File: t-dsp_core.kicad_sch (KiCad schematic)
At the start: 157 parts, among them IC1 Logic Level Shifter - 74HCT2G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, J1 HDR_A_OUTER Teensy-domain, J2 HDR_A_INNER Teensy-domain, J3 HDR_B_OUTER S3-domain, J4 HDR_B_INNER S3-domain, T108 Tab, T109 Tab, T110 Tab, T111 Tab, U1 Teensy 4.1 - DEVKIT, U11 Dual Buffer - SN74LVC2G125DCTR, U13 ESP32-S3-WROOM-1-N16R2, U15 LT3045EMSE#TRPBF, U16 THVD1450DR, U17 ISO7762DW, U18 TEA1-0505HI, U19 SRC4382IPFBR, U20 TLV75718PDRVR, U21 74LVC157APW, U22 IDC777-1, U23 74LVC157APW, U24 AP63203WU, U3 Power Mux & Protect - TPS2116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, U4 Optoisolators - H11L1SM - 6-S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, U5 Dual Buffer - SN74LVC2G125DCTR, U6 Dual Buffer - SN74LVC2G125DCTR, U7 Dual Buffer - SN74LVC2G125DCTR, U8 Dual Buffer - SN74LVC2G125DCTR, U9 Dual Buffer - 74HCT2G17GW,125, Y1 24.576MHz

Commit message: Spin 2 stage 8: DNP/excluded audit and stale notes
- C10/C11 (dnp, excluded) and H1-H4 (excluded) removed
- R19/R53/C4/C5 were excluded-from-board: re-placed on-board at the same
  coordinates with footprints and LCSC numbers; netlist unchanged
- 35 obsolete text notes removed; orphaned GND symbols and hole NC flags removed
- change map section 17

Co-Authored-By: Claude Fable 5.1 <noreply@anthropic.com>
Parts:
- removed C10, C11: 0.1uF, project_fp:C_0805_2012Metric_Pad1.15x1.40mm_HandSolder, symbol TEENSY_4.0_ESP32_AUDIO-rescue:C_Small-Device
- removed C4, C5: 0.1 uF, project_fp:C_0805_2012Metric_Pad1.15x1.40mm_HandSolder, symbol TEENSY_4.0_ESP32_AUDIO-rescue:C_Small-Device
- removed H1, H2, H3, H4: MountingHole_Pad, MountingHole:MountingHole_3.2mm_M3_DIN965_Pad, symbol Mechanical:MountingHole_Pad
- added C4, C5: 0.1 uF, project_fp:C_0805_2012Metric_Pad1.15x1.40mm_HandSolder, symbol Device:C
- R19, R53: LCSC TYPE SMD -> (none); LCSC_MPN 0805W8F1002T5E -> (none); LCSC_Manufacturer UNI-ROYAL -> (none); Package / Case R0805 -> (none)
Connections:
- net ESP32_EN: now also C4.1
- net ESP32_IO0: now also C5.1
- net GND: now also C4.2, C5.2
- no-connect marks 74 -> 70
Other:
- note removed: "3 PIN MIDI"
- note removed: "3.3v DIGITAL RAIL"
- note removed: "5V PRIORITY SWITCHOVER + INRUSH LIMITING"
- note removed: "AUDIO MODULE"
- note removed: "Changed to SPH0645LM4H-B for Target use: Voice/audio capture (speech, speakerphone, voice assistants, etc.)"
- note removed: "ESP32"
- note removed: "ESP32 S3"
- note removed: "ETHERNET"
- note removed: "HAT MOUNTING POINTS"
- note removed: "I2S BUFFER + EXPANSION PORTS"
- note removed: "KiCad 8-Layer Stackup: F.Cu - TOP: Components, ANALOG routes to jacks, ground fill In1.Cu - GND: Solid ground plane In2.Cu - SIG1: TDM/high-speed digital, ground fill In3.Cu - GND: Solid ground plane (isolation!) In4.Cu - SIG2: More TDM/digital signals, ground fill In5.Cu - PWR: Power planes (3.3V/5V) In6.Cu - GND: Solid ground plane B.Cu - BOTTOM: Components, ANALOG routes to jacks, ground fill"
- note removed: "MECHANICAL"
- note removed: "MIDI HEADER"
- note removed: "MUST VERIFY LINES AND PADS"
- note removed: "OPTICAL / TOSLINK IO"
- note removed: "PJRAS2X1S01X INSERT A (RED) RIGHT iNSERT B (WHITE) LEFT"
- note removed: "PLEASE CONFIRM LEFT/RIGHT PINS"
- note removed: "POWER SUPPLY"
- note removed: "RGB LED + HEADER"
- note removed: "SWITCHES"
- note removed: "T-DSP Desktop Soundcard"
- note removed: "TEENSY 4"
- note removed: "TL1105WF160Q = 3.15mm actuator = hidden behind side panel by 1.1mm TL1105XF160Q = 5.85mm actuator = petruding from side panel by 1.35mm ACTUAL DISTANCE FROM EDGE = 4.25mm."
- note removed: "USB A HOST PORT"
- note removed: "USB B Option"
- note removed: "USB C DEVICE PORT"
- note removed: "USB C Option"
- note removed: "USB IN HEADER"
- note removed: "USB POWER FILTER"
- note removed: "https://idyl.io/how-to-add-usb-type-c-micro-usb-replacement/?amp"
- note removed: "https://www.pcbway.com/blog/PCB_Design_Tutorial/How_to_make_your_own_ESP32_breakout_board_with_minimal_circuit.html"
- note removed: "w a0 0a 41 # Configure GPIO1 as PDMCLK with drive active high and low w a0 0d 02 # Configure GPI1 as input"

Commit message: Spin 2 stage 9: function-scoped headers J1-J11 replace the four 2x22 edge blocks; S3 N16R8 (octal PSRAM) frees IO35-37, BT UART RX moves to IO3
Co-Authored-By: Claude Fable 5.1 <noreply@anthropic.com>
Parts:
- removed J1: HDR_A_OUTER Teensy-domain, Connector_PinHeader_2.54mm:PinHeader_2x22_P2.54mm_Vertical, symbol Connector_Generic:Conn_02x22_Odd_Even
- removed J2: HDR_A_INNER Teensy-domain, Connector_PinHeader_2.54mm:PinHeader_2x22_P2.54mm_Vertical, symbol Connector_Generic:Conn_02x22_Odd_Even
- removed J3: HDR_B_OUTER S3-domain, Connector_PinHeader_2.54mm:PinHeader_2x22_P2.54mm_Vertical, symbol Connector_Generic:Conn_02x22_Odd_Even
- removed J4: HDR_B_INNER S3-domain, Connector_PinHeader_2.54mm:PinHeader_2x22_P2.54mm_Vertical, symbol Connector_Generic:Conn_02x22_Odd_Even
- added J1: J_PWR, Connector_PinHeader_2.54mm:PinHeader_2x06_P2.54mm_Vertical, symbol Connector_Generic:Conn_02x06_Odd_Even
- added J10: J_DMX, Connector_PinHeader_2.54mm:PinHeader_1x05_P2.54mm_Vertical, symbol Connector_Generic:Conn_01x05
- added J11: J_LED, Connector_PinHeader_2.54mm:PinHeader_1x05_P2.54mm_Vertical, symbol Connector_Generic:Conn_01x05
- added J2: J_TDM, Connector_PinHeader_2.54mm:PinHeader_2x13_P2.54mm_Vertical, symbol Connector_Generic:Conn_02x13_Odd_Even
- added J3: J_T, Connector_PinHeader_2.54mm:PinHeader_2x12_P2.54mm_Vertical, symbol Connector_Generic:Conn_02x12_Odd_Even
- added J4: J_USBH, Connector_PinHeader_2.54mm:PinHeader_1x05_P2.54mm_Vertical, symbol Connector_Generic:Conn_01x05
- added J5: J_MIDI, Connector_PinHeader_2.54mm:PinHeader_2x04_P2.54mm_Vertical, symbol Connector_Generic:Conn_02x04_Odd_Even
- added J6: J_SPDIF, Connector_PinHeader_2.54mm:PinHeader_2x11_P2.54mm_Vertical, symbol Connector_Generic:Conn_02x11_Odd_Even
- added J7: J_AUX, Connector_PinHeader_2.54mm:PinHeader_2x05_P2.54mm_Vertical, symbol Connector_Generic:Conn_02x05_Odd_Even
- added J8: J_S3, Connector_PinHeader_2.54mm:PinHeader_2x15_P2.54mm_Vertical, symbol Connector_Generic:Conn_02x15_Odd_Even
- added J9: J_USB3, Connector_PinHeader_2.54mm:PinHeader_1x05_P2.54mm_Vertical, symbol Connector_Generic:Conn_01x05
- U13: value ESP32-S3-WROOM-1-N16R2 -> ESP32-S3-WROOM-1-N16R8; LCSC C2913205 -> C2913202; LCSC_MPN ESP32-S3-WROOM-1-N16R2 -> ESP32-S3-WROOM-1-N16R8
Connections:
- net S3_IO3 is gone; now on net BT_UART_RX: U13.15 (IO3)
- net 14_SPDIF_OUT: now also J3.3 (Pin_3)
- net 15_SPDIF_IN: now also J3.4 (Pin_4)
- net 3.3V: now also J1.9 (Pin_9)
- net 3.3V_DIG: now also J1.10 (Pin_10)
- net 32_OUT1B: now also J3.20 (Pin_20)
- net 34_RX8_RESET2: now also J3.10 (Pin_10)
- net 35_TX8_RESET: now also J3.9 (Pin_9)
- net 53_T_PROG: now also J3.11 (Pin_11)
- net 54_ON_OFF: now also J3.12 (Pin_12)
- net 5V: now also J1.5 (Pin_5), J1.6 (Pin_6), J11.5 (Pin_5), J9.5 (Pin_5)
- net 5V_IN: now also J1.1 (Pin_1), J1.2 (Pin_2)
- net 5V_ISO: now also J10.5 (Pin_5)
- net 6_OUT1D+: now also J2.16 (Pin_16)
- net 7_OUT1A+: now also J2.15 (Pin_15)
- net 8_IN1: now also J2.17 (Pin_17)
- net 9_OUT1C_INPUT: now also J2.18 (Pin_18)
- net AUX_I2S_BCK: now also J7.3 (Pin_3)
- net AUX_I2S_DIN: now also J7.7 (Pin_7)
- net AUX_I2S_LRCK: now also J7.6 (Pin_6)
- net AUX_I2S_OUT: now also J7.8 (Pin_8)
- net BCLK1+TDM1: now also J2.7 (Pin_7)
- net BCLK1+TDM2: now also J2.8 (Pin_8)
- net BT_UART_RX: no longer U13.28 (IO35)
- net CRX3: now also J3.7 (Pin_7)
- net CS: now also J8.14 (Pin_14)
- net DC: now also J8.17 (Pin_17)
- net DMX_A: now also J10.2 (Pin_2)
- net DMX_B: now also J10.3 (Pin_3)
- net DMX_GND: now also J10.1 (Pin_1), J10.4 (Pin_4)
- net ESP32_EN: now also J8.5 (Pin_5)
- net ESP32_IO0: now also J8.6 (Pin_6)
- net ESP32_IO1: now also J8.3 (Pin_3)
- net ESP32_IO21_SDA: now also J8.9 (Pin_9)
- net ESP32_IO22_SCL: now also J8.10 (Pin_10)
- net ESP32_IO3: now also J8.4 (Pin_4)
- net ESP32_LED_OUT: now also J11.4 (Pin_4)
- net GND: now also J1.12 (Pin_12), J1.3 (Pin_3), J1.4 (Pin_4), J1.7 (Pin_7), J1.8 (Pin_8), J11.1 (Pin_1), J11.3 (Pin_3), J2.1 (Pin_1), J2.10 (Pin_10), J2.13 (Pin_13), J2.14 (Pin_14), J2.19 (Pin_19), J2.2 (Pin_2), J2.20 (Pin_20), J2.25 (Pin_25), J2.26 (Pin_26), J2.5 (Pin_5), J2.6 (Pin_6), J2.9 (Pin_9), J3.1 (Pin_1), J3.15 (Pin_15), J3.16 (Pin_16), J3.2 (Pin_2), J3.21 (Pin_21), J3.23 (Pin_23), J3.24 (Pin_24), J3.5 (Pin_5), J3.6 (Pin_6), J4.1 (Pin_1), J4.4 (Pin_4), J5.7 (Pin_7), J5.8 (Pin_8), J6.1 (Pin_1), J6.10 (Pin_10), J6.13 (Pin_13), J6.14 (Pin_14), J6.17 (Pin_17), J6.18 (Pin_18), J6.2 (Pin_2), J6.21 (Pin_21), J6.22 (Pin_22), J6.5 (Pin_5), J6.6 (Pin_6), J6.9 (Pin_9), J7.1 (Pin_1), J7.10 (Pin_10), J7.2 (Pin_2), J7.4 (Pin_4), J7.5 (Pin_5), J7.9 (Pin_9), J8.1 (Pin_1), J8.15 (Pin_15), J8.16 (Pin_16), J8.2 (Pin_2), J8.23 (Pin_23), J8.24 (Pin_24), J8.28 (Pin_28), J8.29 (Pin_29), J8.30 (Pin_30), J8.7 (Pin_7), J8.8 (Pin_8), J9.1 (Pin_1), J9.4 (Pin_4)
- net GPIO34: now also J8.25 (Pin_25)
- net GPIO35: now also J8.26 (Pin_26)
- net HOST_5V: now also J4.5 (Pin_5)
- net HOST_D1+: now also J4.3 (Pin_3)
- net HOST_D1-: now also J4.2 (Pin_2)
- net LRCK1+TDM1: now also J2.11 (Pin_11)
- net LRCK1+TDM2: now also J2.12 (Pin_12)
- net MCLK1+TDM1: now also J2.3 (Pin_3)
- net MCLK1+TDM2: now also J2.4 (Pin_4)
- net MCLK2: now also J3.22 (Pin_22)
- net MIDI_IN_4: now also J5.1 (Pin_1)
- net MIDI_IN_5: now also J5.2 (Pin_2)
- net MIDI_OUT_4: now also J5.3 (Pin_3)
- net MIDI_OUT_5: now also J5.4 (Pin_4)
- net MIDI_THRU_4: now also J5.5 (Pin_5)
- net MIDI_THRU_5: now also J5.6 (Pin_6)
- net OUTPUTA: now also J8.20 (Pin_20)
- net OUTPUTB: now also J8.21 (Pin_21)
- net RESET: now also J8.18 (Pin_18)
- net S3_IO45: now also J8.27 (Pin_27)
- net S3_USB_DN: now also J9.2 (Pin_2)
- net S3_USB_DP: now also J9.3 (Pin_3)
- net SCK: now also J8.11 (Pin_11)
- net SCL0: now also J2.23 (Pin_23)
- net SCL1: now also J2.24 (Pin_24)
- net SDA0: now also J2.21 (Pin_21)
- net SDA1: now also J2.22 (Pin_22)
- net SDI: now also J8.12 (Pin_12)
- net SDO: now also J8.13 (Pin_13)
- net SPDIF_RX1N: now also J6.4 (Pin_4)
- net SPDIF_RX1P: now also J6.3 (Pin_3)
- net SPDIF_RX2N: now also J6.8 (Pin_8)
- net SPDIF_RX2P: now also J6.7 (Pin_7)
- net SPDIF_RX3N: now also J6.12 (Pin_12)
- net SPDIF_RX3P: now also J6.11 (Pin_11)
- net SPDIF_RX4N: now also J6.16 (Pin_16)
- net SPDIF_RX4P: now also J6.15 (Pin_15)
- net SPDIF_TXN: now also J6.20 (Pin_20)
- net SPDIF_TXP: now also J6.19 (Pin_19)
- net SWITCH: now also J8.22 (Pin_22)
- net TEENSY_LED_OUT: now also J11.2 (Pin_2)
- net TRX3: now also J3.8 (Pin_8)
- net T_22: now also J3.17 (Pin_17)
- net T_26: now also J3.18 (Pin_18)
- net T_27: now also J3.19 (Pin_19)
- net T_BUTTON1: now also J3.13 (Pin_13)
- net T_BUTTON2: now also J3.14 (Pin_14)
- net T_CS: now also J8.19 (Pin_19)
- net V_BAT: now also J1.11 (Pin_11)
- net S3_IO36: no longer names the net of U13.29 (IO36)
- net S3_IO37: no longer names the net of U13.30 (IO37)
- no-connect marks 70 -> 60

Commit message: Spin 2 stage 9b: J12 J_ETH header, PSRAM and Ethernet notes on the sheet, change map sections 3/10/11/13/14/15 rewritten for the function-scoped headers
Co-Authored-By: Claude Fable 5.1 <noreply@anthropic.com>
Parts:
- added J12: J_ETH, Connector_PinHeader_2.54mm:PinHeader_2x04_P2.54mm_Vertical, symbol Connector_Generic:Conn_02x04_Odd_Even
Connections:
- net GND: now also J12.3 (Pin_3), J12.4 (Pin_4), J12.8 (Pin_8)
- new net ETH_LED: J12.7 (Pin_7)
- new net ETH_R+: J12.1 (Pin_1)
- new net ETH_R-: J12.2 (Pin_2)
- new net ETH_T+: J12.5 (Pin_5)
- new net ETH_T-: J12.6 (Pin_6)
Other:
- note added: "J_ETH: Teensy 4.1 Ethernet pads 60-65 (R+ R- T+ T- LED GND, 2 mm 2x3 on the Teensy bottom).\nPENDING: change U1 to project_sch:Teensy4.1 in eeschema, label pins 60=ETH_R+ 61=ETH_LED 62=ETH_T- 63=ETH_T+ 64=GND 65=ETH_R-,\nand restore pads 60-65 in Teensy41_mod3 (they exist in Teensy41.kicad_mod). Magnetics + RJ45 live on the backplane."
- note added: "U1 Teensy 4.1 memory: fit 2x APS6404L-3SQR-SN (8 MB PSRAM each, 16 MB total, EXTMEM) on the Teensy's own bottom-side SOIC-8 pads\nfor loop recording, echo and reverb buffers. Optional W25Q128 QSPI flash on the second pad if 8 MB PSRAM + flash is preferred.\nPCB rule: no parts or pads on the core top side under the Teensy footprint (SOIC-8 bodies 1.2 mm tall); Teensy sits on 2.54 mm headers."
- note added: "U13 = ESP32-S3-WROOM-1-N16R8 (16 MB flash + 8 MB OCTAL PSRAM, needed for Spotify/cspot stream buffering).\nOctal PSRAM owns IO35/IO36/IO37 -> those module pins are NC. BT UART RX therefore uses IO3 (not IO35).\nDo not substitute an R2 (quad) module without re-checking: R2 frees IO35-37 but 2 MB PSRAM is too small for Spotify."

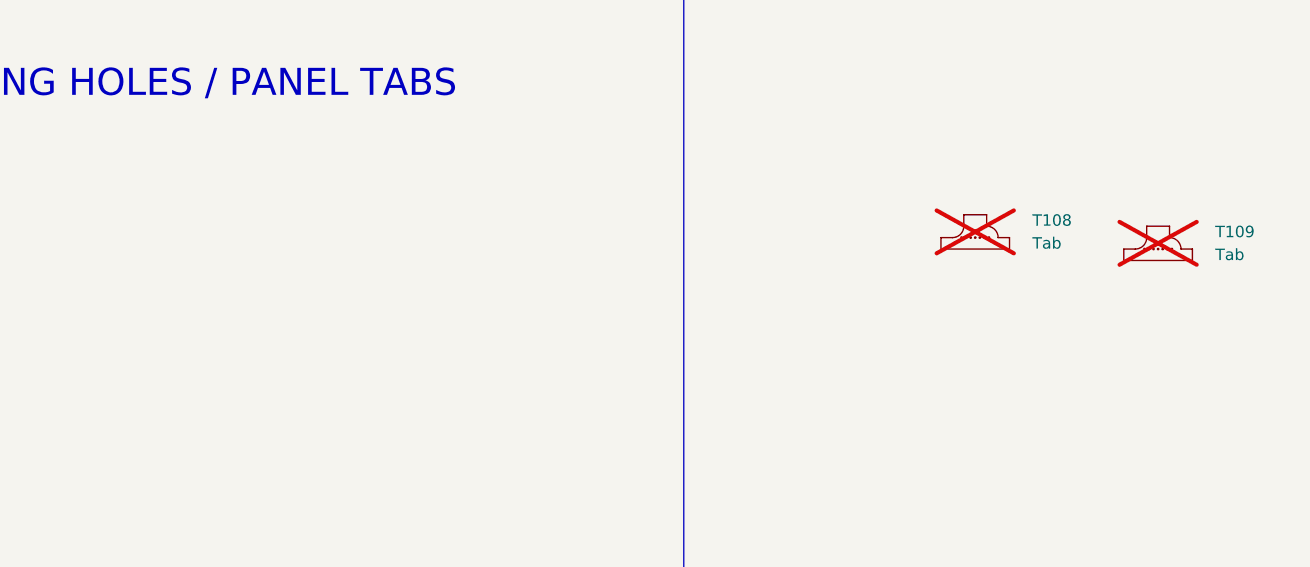
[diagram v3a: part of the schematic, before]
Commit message: Spin 2 stage 10b: H1-H4 M3 mounting holes in the schematic (KiCad discarded the PCB-only holes); change map note
Co-Authored-By: Claude Fable 5.1 <noreply@anthropic.com>
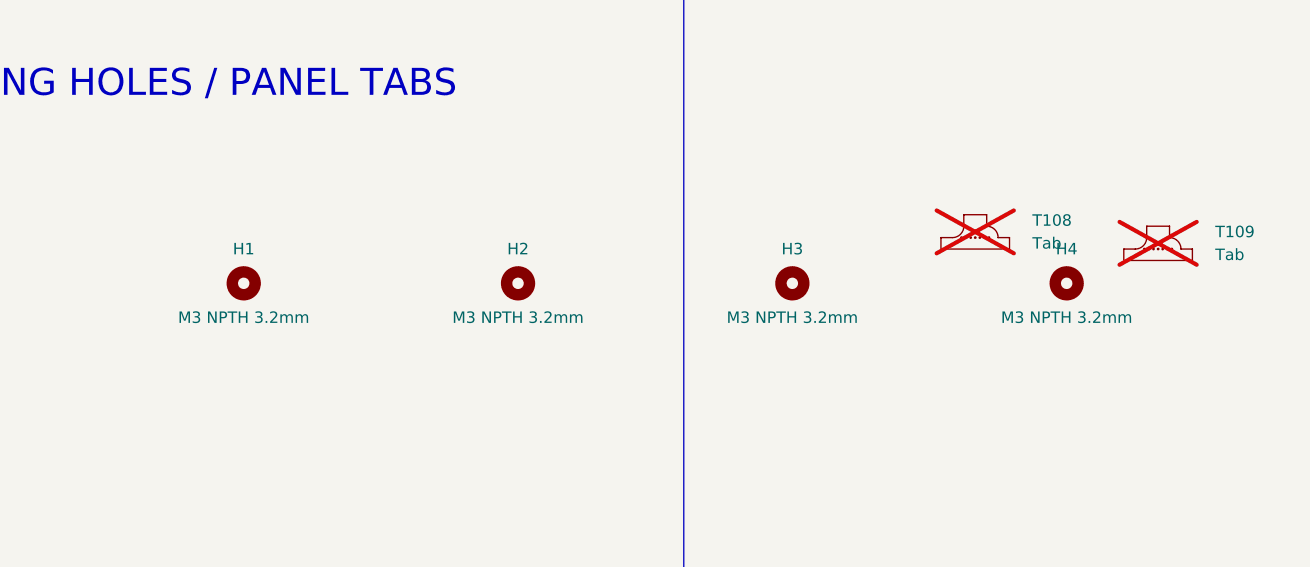
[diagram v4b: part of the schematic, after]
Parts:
- added H1, H2, H3, H4: M3 NPTH 3.2mm, MountingHole:MountingHole_3.2mm_M3, symbol Mechanical:MountingHole
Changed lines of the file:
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@@
         (size 3 3)))
 )
+  (text "J_ETH: Teensy 4.1 Ethernet pads 60-65 (R+ R- T+ T- LED GND, 2 mm 2x3 on the Teensy bottom).\\nPENDING: change U1 to project_sch:Teensy4.1 in eeschema, label pins 60=ETH_R+ 61=ETH_LED 62=ETH_T- 63=ETH_T+ 64=GND 65=ETH_R-,\\nand restore pads 60-65 in Teensy41_mod3 (they exist in Teensy41.kicad_mod). Magnetics + RJ45 live on the backplane."
+    (at 560.07 300.99 0)
+    (effects
+      (font
+        (size 1.27 1.27)))
+)
+  (text "U13 = ESP32-S3-WROOM-1-N16R8 (16 MB flash + 8 MB OCTAL PSRAM, needed for Spotify/cspot stream buffering).\\nOctal PSRAM owns IO35/IO36/IO37 -> those module pins are NC. BT UART RX therefore uses IO3 (not IO35).\\nDo not substitute an R2 (quad) module without re-checking: R2 frees IO35-37 but 2 MB PSRAM is too small for Spotify."
+    (at -320.04 570.23 0)
+    (effects
+      (font
+        (size 1.27 1.27)))
+)
+  (text "U1 Teensy 4.1 memory: fit 2x APS6404L-3SQR-SN (8 MB PSRAM each, 16 MB total, EXTMEM) on the Teensy's own bottom-side SOIC-8 pads\\nfor loop recording, echo and reverb buffers. Optional W25Q128 QSPI flash on the second pad if 8 MB PSRAM + flash is preferred.\\nPCB rule: no parts or pads on the core top side under the Teensy footprint (SOIC-8 bodies 1.2 mm tall); Teensy sits on 2.54 mm headers."
+    (at 95.25 338.14 0)
+    (effects
+      (font
+        (size 1.27 1.27)))
+)
   (label "DMX_RO_ISO"
     (at -224.79 924.56 0)
@@
           (reference "J12")
           (unit 1)))))
+  (symbol
+    (lib_id "Mechanical:MountingHole")
+    (at 1029.97 640.08 0)
+    (unit 1)
+    (in_bom yes)
+    (on_board yes)
+    (dnp no)
+    (property "Reference" "H1"
+      (at 1029.97 636.27 0)
+      (effects
+        (font
+          (size 1.27 1.27))))
+    (property "Value" "M3 NPTH 3.2mm"
+      (at 1029.97 643.89 0)
+      (effects
+        (font
+          (size 1.27 1.27))))
+    (property "Footprint" "MountingHole:MountingHole_3.2mm_M3"
+      (at 1029.97 640.08 0)
+      (effects
+        (font
+          (size 1.27 1.27))
+        (hide yes)))
+    (property "Datasheet" ""
+      (at 1029.97 640.08 0)
+      (effects
+        (font
+          (size 1.27 1.27))
+        (hide yes)))
+    (instances
+      (project "t-dsp_core"
+        (path "/6a0ff39d-771d-410f-9e7c-006586d81d16"
+          (reference "H1")
+          (unit 1)))))
+  (symbol
+    (lib_id "Mechanical:MountingHole")
+    (at 1060.45 640.08 0)
+    (unit 1)
+    (in_bom yes)
+    (on_board yes)
+    (dnp no)
+    (property "Reference" "H2"
+      (at 1060.45 636.27 0)
+      (effects
+        (font
+          (size 1.27 1.27))))
+    (property "Value" "M3 NPTH 3.2mm"
+      (at 1060.45 643.89 0)
+      (effects
+        (font
+          (size 1.27 1.27))))
+    (property "Footprint" "MountingHole:MountingHole_3.2mm_M3"
+      (at 1060.45 640.08 0)
+      (effects
+        (font
+          (size 1.27 1.27))
+        (hide yes)))
+    (property "Datasheet" ""
+      (at 1060.45 640.08 0)
+      (effects
+        (font
+          (size 1.27 1.27))
+        (hide yes)))
+    (instances
+      (project "t-dsp_core"
+        (path "/6a0ff39d-771d-410f-9e7c-006586d81d16"
+          (reference "H2")
+          (unit 1)))))
+  (symbol
+    (lib_id "Mechanical:MountingHole")
+    (at 1090.93 640.08 0)
+    (unit 1)
+    (in_bom yes)
+    (on_board yes)
+    (dnp no)
+    (property "Reference" "H3"
+      (at 1090.93 636.27 0)
+      (effects
+        (font
+          (size 1.27 1.27))))
+    (property "Value" "M3 NPTH 3.2mm"
+      (at 1090.93 643.89 0)
+      (effects
+        (font
+          (size 1.27 1.27))))
+    (property "Footprint" "MountingHole:MountingHole_3.2mm_M3"
+      (at 1090.93 640.08 0)
+      (effects
+        (font
+          (size 1.27 1.27))
+        (hide yes)))
+    (property "Datasheet" ""
+      (at 1090.93 640.08 0)
+      (effects
+        (font
+          (size 1.27 1.27))
+        (hide yes)))
+    (instances
+      (project "t-dsp_core"
+        (path "/6a0ff39d-771d-410f-9e7c-006586d81d16"
+          (reference "H3")
+          (unit 1)))))
+  (symbol
+    (lib_id "Mechanical:MountingHole")
+    (at 1121.41 640.08 0)
+    (unit 1)
+    (in_bom yes)
+    (on_board yes)
+    (dnp no)
+    (property "Reference" "H4"
+      (at 1121.41 636.27 0)
+      (effects
+        (font
+          (size 1.27 1.27))))
+    (property "Value" "M3 NPTH 3.2mm"
+      (at 1121.41 643.89 0)
+      (effects
+        (font
+          (size 1.27 1.27))))
+    (property "Footprint" "MountingHole:MountingHole_3.2mm_M3"
+      (at 1121.41 640.08 0)
+      (effects
+        (font
+          (size 1.27 1.27))
+        (hide yes)))
+    (property "Datasheet" ""
+      (at 1121.41 640.08 0)
+      (effects
+        (font
+          (size 1.27 1.27))
+        (hide yes)))
+    (instances
+      (project "t-dsp_core"
+        (path "/6a0ff39d-771d-410f-9e7c-006586d81d16"
+          (reference "H4")
+          (unit 1)))))
   (rectangle
     (start 1008.38 845.82)
@@
     (path "/"
       (page "1")))
-  (text "J_ETH: Teensy 4.1 Ethernet pads 60-65 (R+ R- T+ T- LED GND, 2 mm 2x3 on the Teensy bottom).\\nPENDING: change U1 to project_sch:Teensy4.1 in eeschema, label pins 60=ETH_R+ 61=ETH_LED 62=ETH_T- 63=ETH_T+ 64=GND 65=ETH_R-,\\nand restore pads 60-65 in Teensy41_mod3 (they exist in Teensy41.kicad_mod). Magnetics + RJ45 live on the backplane."
-    (at 560.07 300.99 0)
-    (effects (font (size 1.27 1.27)))
-  )
-  (text "U13 = ESP32-S3-WROOM-1-N16R8 (16 MB flash + 8 MB OCTAL PSRAM, needed for Spotify/cspot stream buffering).\\nOctal PSRAM owns IO35/IO36/IO37 -> those module pins are NC. BT UART RX therefore uses IO3 (not IO35).\\nDo not substitute an R2 (quad) module without re-checking: R2 frees IO35-37 but 2 MB PSRAM is too small for Spotify."
-    (at -320.04 570.23 0)
-    (effects (font (size 1.27 1.27)))
-  )
-  (text "U1 Teensy 4.1 memory: fit 2x APS6404L-3SQR-SN (8 MB PSRAM each, 16 MB total, EXTMEM) on the Teensy's own bottom-side SOIC-8 pads\\nfor loop recording, echo and reverb buffers. Optional W25Q128 QSPI flash on the second pad if 8 MB PSRAM + flash is preferred.\\nPCB rule: no parts or pads on the core top side under the Teensy footprint (SOIC-8 bodies 1.2 mm tall); Teensy sits on 2.54 mm headers."
-    (at 95.25 338.14 0)
-    (effects (font (size 1.27 1.27)))
-  ))
+)
